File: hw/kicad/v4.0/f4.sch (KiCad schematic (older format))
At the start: 37 parts, among them P1 USB_OTG, U1 USBLC6-4SC6, U20 USBLC6-4SC6, U22 USBLC6-4SC6, U23 USBLC6-4SC6, U26 STM32F405VG, Y2 8M

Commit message: update TVS LCSC part number
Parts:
- U1, U20, U22, U23: LCSC C252436 -> C435848
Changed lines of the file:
@@
 EESchema Schematic File Version 4
-LIBS:stmbl_4.0-cache
 EELAYER 30 0
 EELAYER END
@@
 F 9 "" H 0   0   50  0001 C CNN "Voltage"
 F 10 "STMicroelectronics" H 0   0   50  0001 C CNN "Manufacturer"
-F 11 "C252436" H 2800 6550 50  0001 C CNN "LCSC"
+F 11 "C435848" H 2800 6550 50  0001 C CNN "LCSC"
 	1    2800 6550
 	1    0    0    -1
@@
 F 9 "" H 0   0   50  0001 C CNN "Voltage"
 F 10 "STMicroelectronics" H 0   0   50  0001 C CNN "Manufacturer"
-F 11 "C252436" H 4600 10150 50  0001 C CNN "LCSC"
+F 11 "C435848" H 4600 10150 50  0001 C CNN "LCSC"
 	1    4600 10150
 	1    0    0    -1
@@
 F 9 "" H 0   0   50  0001 C CNN "Voltage"
 F 10 "STMicroelectronics" H 0   0   50  0001 C CNN "Manufacturer"
-F 11 "C252436" H 2800 1950 50  0001 C CNN "LCSC"
+F 11 "C435848" H 2800 1950 50  0001 C CNN "LCSC"
 	1    2800 1950
 	-1   0    0    -1
@@
 F 9 "" H 0   0   50  0001 C CNN "Voltage"
 F 10 "STMicroelectronics" H 0   0   50  0001 C CNN "Manufacturer"
-F 11 "C252436" H 2800 2650 50  0001 C CNN "LCSC"
+F 11 "C435848" H 2800 2650 50  0001 C CNN "LCSC"
 	1    2800 2650
 	-1   0    0    -1

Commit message: Changed 120uf 1808 to 1210 100uF
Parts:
- C1, C119, C16, C29, C61, C66, C67, C77, C80, C84, C85, C86, C87, C89: LCSC C14663 -> C14663
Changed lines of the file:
@@
 F 9 "" H 0   0   50  0001 C CNN "Description"
 F 10 "" H 0   0   50  0001 C CNN "Manufacturer"
-F 11 " C14663" H 11400 2150 50  0001 C CNN "LCSC"
+F 11 "C14663" H 11400 2150 50  0001 C CNN "LCSC"
 	1    11400 2150
 	1    0    0    -1
@@
 F 9 "" H 0   0   50  0001 C CNN "Description"
 F 10 "" H 0   0   50  0001 C CNN "Manufacturer"
-F 11 " C14663" H 10900 2150 50  0001 C CNN "LCSC"
+F 11 "C14663" H 10900 2150 50  0001 C CNN "LCSC"
 	1    10900 2150
 	1    0    0    -1
@@
 F 9 "" H 0   0   50  0001 C CNN "Description"
 F 10 "" H 0   0   50  0001 C CNN "Manufacturer"
-F 11 " C14663" H 10600 2150 50  0001 C CNN "LCSC"
+F 11 "C14663" H 10600 2150 50  0001 C CNN "LCSC"
 	1    10600 2150
 	1    0    0    -1
@@
 F 9 "" H 0   0   50  0001 C CNN "Description"
 F 10 "" H 0   0   50  0001 C CNN "Manufacturer"
-F 11 " C14663" H 10300 2150 50  0001 C CNN "LCSC"
+F 11 "C14663" H 10300 2150 50  0001 C CNN "LCSC"
 	1    10300 2150
 	1    0    0    -1
@@
 F 9 "" H 0   0   50  0001 C CNN "Description"
 F 10 "" H 0   0   50  0001 C CNN "Manufacturer"
-F 11 " C14663" H 10000 2150 50  0001 C CNN "LCSC"
+F 11 "C14663" H 10000 2150 50  0001 C CNN "LCSC"
 	1    10000 2150
 	1    0    0    -1
@@
 F 9 "" H 0   0   50  0001 C CNN "Description"
 F 10 "" H 0   0   50  0001 C CNN "Manufacturer"
-F 11 " C14663" H 9700 2150 50  0001 C CNN "LCSC"
+F 11 "C14663" H 9700 2150 50  0001 C CNN "LCSC"
 	1    9700 2150
 	1    0    0    -1
@@
 F 9 "" H 0   0   50  0001 C CNN "Description"
 F 10 "" H 0   0   50  0001 C CNN "Manufacturer"
-F 11 " C14663" H 9400 2150 50  0001 C CNN "LCSC"
+F 11 "C14663" H 9400 2150 50  0001 C CNN "LCSC"
 	1    9400 2150
 	1    0    0    -1
@@
 F 9 "" H 0   0   50  0001 C CNN "Description"
 F 10 "" H 0   0   50  0001 C CNN "Manufacturer"
-F 11 " C14663" H 4600 2850 50  0001 C CNN "LCSC"
+F 11 "C14663" H 4600 2850 50  0001 C CNN "LCSC"
 	1    4600 2850
 	1    0    0    -1
@@
 F 9 "" H 0   0   50  0001 C CNN "Description"
 F 10 "" H 0   0   50  0001 C CNN "Manufacturer"
-F 11 " C14663" H 2800 7050 50  0001 C CNN "LCSC"
+F 11 "C14663" H 2800 7050 50  0001 C CNN "LCSC"
 	1    2800 7050
 	0    1    1    0
@@
 F 9 "" H 0   0   50  0001 C CNN "Description"
 F 10 "" H 0   0   50  0001 C CNN "Manufacturer"
-F 11 " C14663" H 8100 2150 50  0001 C CNN "LCSC"
+F 11 "C14663" H 8100 2150 50  0001 C CNN "LCSC"
 	1    8100 2150
 	1    0    0    -1
@@
 F 9 "" H 0   0   50  0001 C CNN "Description"
 F 10 "" H 0   0   50  0001 C CNN "Manufacturer"
-F 11 " C14663" H 850 6650 50  0001 C CNN "LCSC"
+F 11 "C14663" H 850 6650 50  0001 C CNN "LCSC"
 	1    850  6650
 	1    0    0    -1
@@
 F 9 "" H 0   0   50  0001 C CNN "Description"
 F 10 "" H 0   0   50  0001 C CNN "Manufacturer"
-F 11 " C14663" H 2150 3450 50  0001 C CNN "LCSC"
+F 11 "C14663" H 2150 3450 50  0001 C CNN "LCSC"
 	1    2150 3450
 	1    0    0    -1
@@
 F 9 "" H 0   0   50  0001 C CNN "Description"
 F 10 "" H 0   0   50  0001 C CNN "Manufacturer"
-F 11 " C14663" H 2600 3450 50  0001 C CNN "LCSC"
+F 11 "C14663" H 2600 3450 50  0001 C CNN "LCSC"
 	1    2600 3450
 	1    0    0    -1
@@
 F 9 "" H 0   0   50  0001 C CNN "Description"
 F 10 "" H 0   0   50  0001 C CNN "Manufacturer"
-F 11 " C14663" H 4750 9250 50  0001 C CNN "LCSC"
+F 11 "C14663" H 4750 9250 50  0001 C CNN "LCSC"
 	1    4750 9250
 	1    0    0    -1

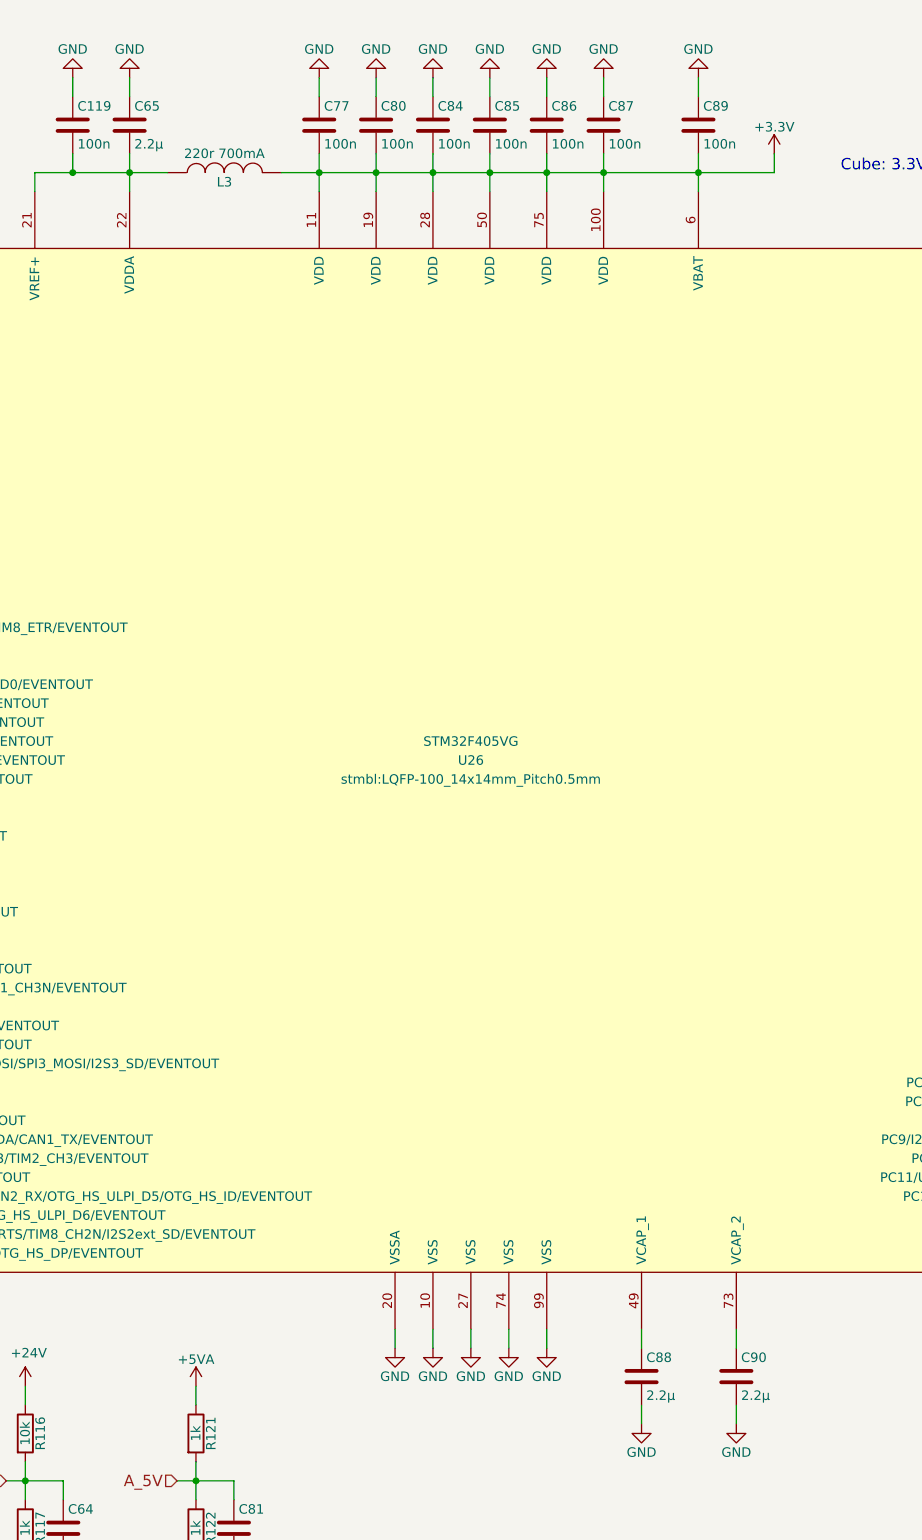
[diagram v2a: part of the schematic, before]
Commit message: Switch some 2.2uf 0603 to 1uf bypass to get 50V version on jlcpcb
Change 2.2uf 0603 to 0805 on iram to get 50V version on jlcpcb
other cleanup
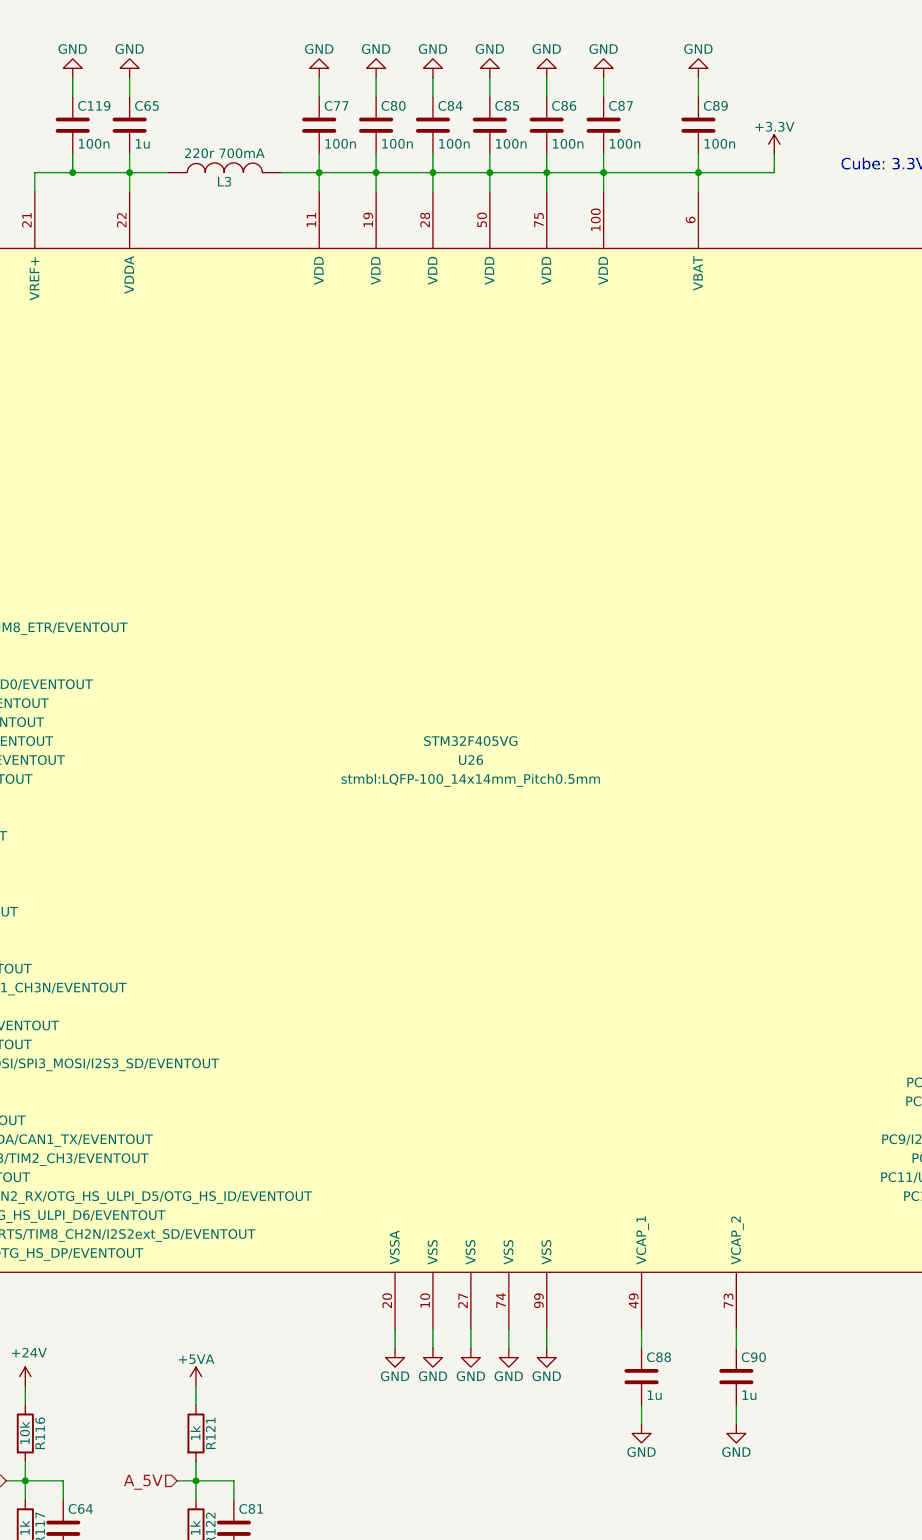
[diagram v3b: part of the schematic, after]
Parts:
- C1, C119, C16, C29, C61, C66, C67, C77, C80, C84, C85, C86, C87, C89: Manufacturer (none) -> YAGEO; Manufacturer No (none) -> CC0603KRX7R9BB104
- C31, C32: Manufacturer (none) -> Samsung Electro-Mechanics; Manufacturer No (none) -> CL10C180JB8NNNC
- C64, C81: Manufacturer (none) -> Samsung Electro-Mechanics; Manufacturer No (none) -> CL10B102KB8NNNC
- C65, C88, C90: value 2.2µ -> 1u; LCSC C23630 -> C15849; Manufacturer (none) -> Samsung Electro-Mechanics; Manufacturer No (none) -> CL10A105KB8NNNC

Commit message: Change Crystals to right footprint
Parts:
- Y2: LCSC C389778 -> C157341
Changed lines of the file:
@@
 F 9 "" H 0   0   50  0001 C CNN "Description"
 F 10 "Abracon LLC" H 0   0   50  0001 C CNN "Manufacturer"
-F 11 "C389778" H 4700 3700 50  0001 C CNN "LCSC"
+F 11 "C157341" H 4700 3700 50  0001 C CNN "LCSC"
 	1    4700 3700
 	0    1    1    0
